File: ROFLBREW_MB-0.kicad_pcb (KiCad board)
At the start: 4 copper layers, 132.7 x 76 mm, 453 parts, among them P1 CONN_01X02, P10 CONN_01X02, P11 CONN_01X02, P12 CONN_01X02, P13 CONN_02X03, P14 CONN_01X02, P15 CONN_01X02, P16 CONN_01X02, P17 CONN_01X02, P18 CONN_01X02, P19 CONN_01X02, P2 CONN_01X02, P20 CONN_01X02, P21 CONN_02X20, P22 CONN_02X04, P23 CONN_02X04, P24 CONN_01X02, P25 CONN_01X02, P26 CONN_01X02, P27 CONN_01X02, P28 CONN_01X02, P29 CONN_01X02, P3 CONN_01X02, P30 CONN_01X02, P31 CONN_01X02, P4 CONN_01X02, P5 CONN_02X10, P6 CONN_01X02, P7 CONN_02X08, P8 CONN_01X02, P9 CONN_01X02, Q1 ASEM1, Q2 MUN5233T1G, Q3 ASTMTXK, U1 LT3480, U2 STM32F756ZGTx, U3 MAX31865, U4 MAX31865, U5 MAX31865, U6 MAX31865

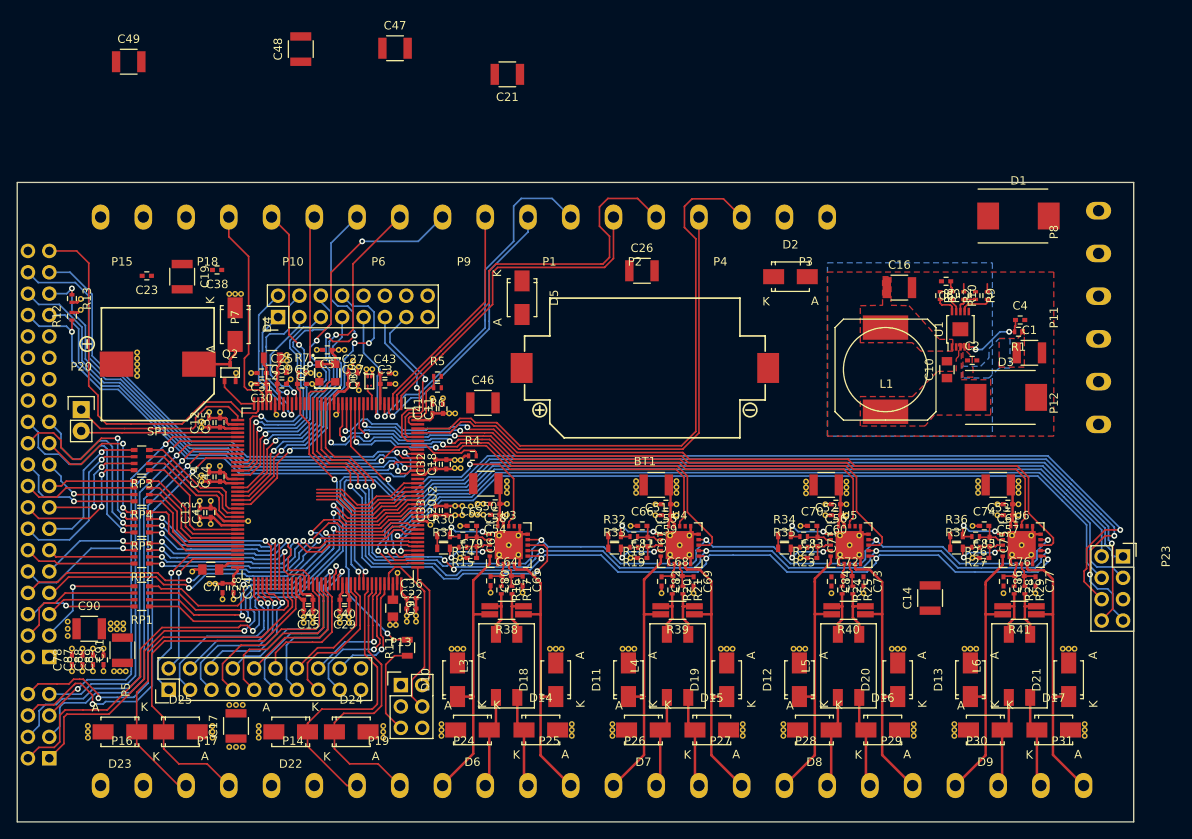
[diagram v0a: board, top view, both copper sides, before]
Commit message: Update some component footprints, add SD card and RTD power routing
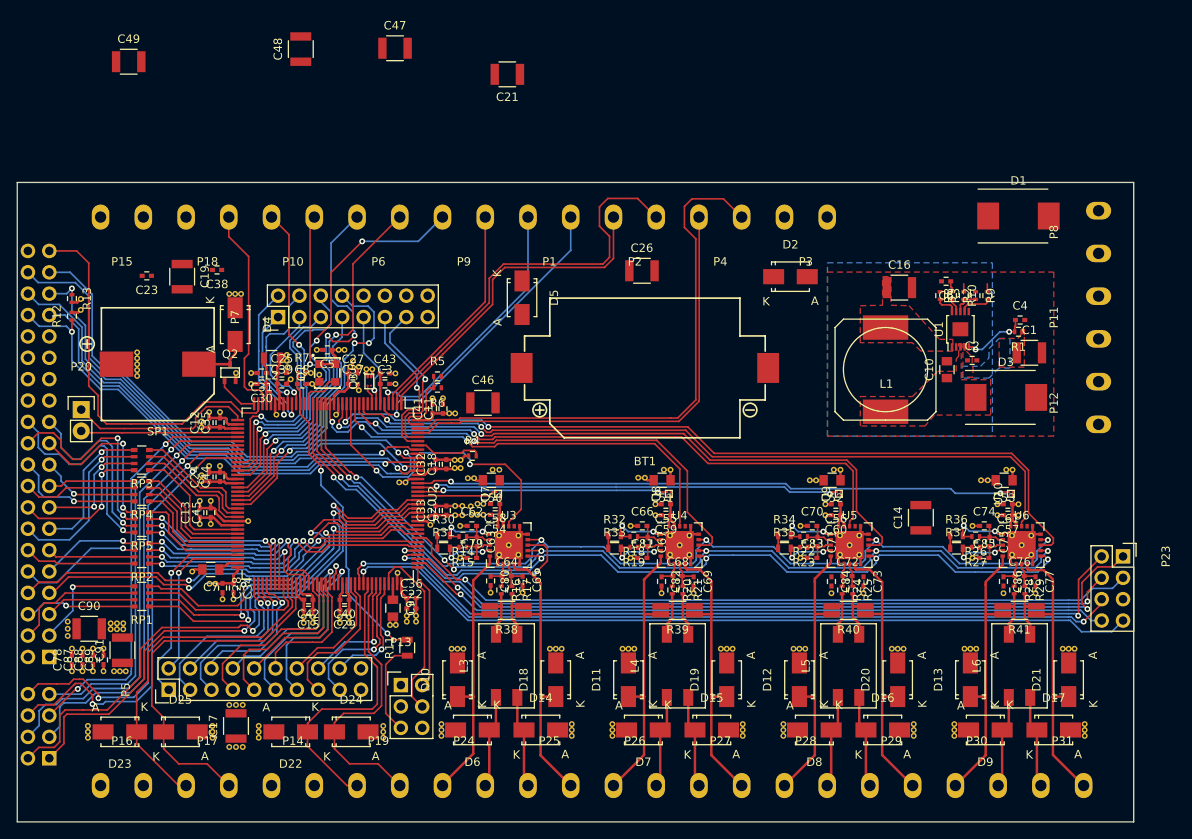
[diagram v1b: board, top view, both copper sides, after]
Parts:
- removed the REF** at (149.2, 101.9)
- removed the REF** at (128.8, 102.0)
- removed the REF** at (113.3, 101.7)
- removed the REF** at (108.5, 101.9)
- removed the REF** at (154.0, 102.4)
- removed the REF** at (154.0, 101.7)
- removed the REF** at (154.0, 101.0)
- removed the REF** at (133.6, 102.5)
- removed the REF** at (133.6, 101.8)
- removed the REF** at (133.6, 101.0)
- removed the REF** at (133.6, 105.0)
- removed the REF** at (133.6, 103.8)
- removed the REF** at (113.3, 105.0)
- removed the REF** at (113.3, 103.8)
- removed the REF** at (113.3, 102.4)
- removed the REF** at (113.3, 101.8)
- removed the REF** at (93.2, 104.5)
- removed the REF** at (93.2, 103.2)
- removed the REF** at (93.2, 100.5)
- added REF**: VIA-0.7x0.35, vias:VIA-0.7x0.35, F.Cu at (80.4, 100.7)
- added REF**: VIA-0.7x0.35, vias:VIA-0.7x0.35, F.Cu at (81.2, 100.7)
- added REF**: VIA-0.7x0.35, vias:VIA-0.7x0.35, F.Cu at (152.6, 99.2)
- added REF**: VIA-0.7x0.35, vias:VIA-0.7x0.35, F.Cu at (153.3, 99.2)
- added REF**: VIA-0.7x0.35, vias:VIA-0.7x0.35, F.Cu at (132.1, 99.2)
- added REF**: VIA-0.7x0.35, vias:VIA-0.7x0.35, F.Cu at (132.8, 99.2)
- added REF**: VIA-0.7x0.35, vias:VIA-0.7x0.35, F.Cu at (112.7, 99.2)
- added REF**: VIA-0.7x0.35, vias:VIA-0.7x0.35, F.Cu at (88.5, 100.2)
- added REF**: VIA-0.7x0.35, vias:VIA-0.7x0.35, F.Cu at (89.3, 100.2)
- added U10: TPS2290x, power_switches:TPS229x, F.Cu at (153.1, 102.0)
- added U7: TPS2290x, power_switches:TPS229x, F.Cu at (92.2, 102.0)
- added U8: TPS2290x, power_switches:TPS229x, F.Cu at (112.5, 102.0)
- added U9: TPS2290x, power_switches:TPS229x, F.Cu at (132.7, 102.0)
- C50, C51, C52, C53: value 22µ -> 1µ; footprint Capacitors_SMD:C_1210 -> Capacitors_SMD:C_0805
- moved C14 9.61 mm to (142.4, 104.8)
- moved REF** 2.89 mm to (92.3, 99.2)
- moved REF** 2.66 mm to (91.5, 99.2)
- moved REF** 2.02 mm to (111.8, 99.2)
- moved REF** 1.21 mm to (129.9, 100.4)
- moved REF** 1.15 mm to (150.3, 100.4)
- moved REF** 1.13 mm to (108.8, 100.1)
- moved REF** 1.12 mm to (109.6, 100.1)
- moved REF** 0.96 mm to (129.2, 100.4)
- moved C53 0.89 mm to (152.3, 100.4)
- moved C51 0.89 mm to (111.7, 100.4)
- moved C52 0.89 mm to (131.8, 100.4)
- moved REF** 0.87 mm to (149.6, 100.4)
- moved C50 0.76 mm to (91.3, 100.4)
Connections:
- C54 pad 1: +3V3 -> Net-(C54-Pad1)
- C55 pad 1: +3V3 -> Net-(C55-Pad1)
- C56 pad 1: +3V3 -> Net-(C56-Pad1)
- C57 pad 1: +3V3 -> Net-(C57-Pad1)
- C58 pad 1: +3V3 -> Net-(C54-Pad1)
- C59 pad 1: +3V3 -> Net-(C55-Pad1)
- C60 pad 1: +3V3 -> Net-(C56-Pad1)
- C61 pad 1: +3V3 -> Net-(C57-Pad1)
- P5 pad 19: /PG11 -> Net-(P5-Pad19)
- P5 pad 20: /PG12 -> Net-(P5-Pad20)
- P7 pad 10: /PG14 -> Net-(P7-Pad10)
- P7 pad 12: /PG13 -> Net-(P7-Pad12)
- U2 pad 126: /PG11 -> /RTD_PWR_0
- U2 pad 127: /PG12 -> /RTD_PWR_1
- U2 pad 128: /PG13 -> /RTD_PWR_2
- U2 pad 129: /PG14 -> /RTD_PWR_3
- U3 pad 19: +3V3 -> Net-(C54-Pad1)
- U3 pad 20: +3V3 -> Net-(C54-Pad1)
- U4 pad 19: +3V3 -> Net-(C55-Pad1)
- U4 pad 20: +3V3 -> Net-(C55-Pad1)
- U5 pad 19: +3V3 -> Net-(C56-Pad1)
- U5 pad 20: +3V3 -> Net-(C56-Pad1)
- U6 pad 19: +3V3 -> Net-(C57-Pad1)
- U6 pad 20: +3V3 -> Net-(C57-Pad1)
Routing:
- net /RTD_PWR_3: track 0.00 -> 71.1 mm, vias 0 -> 2
- net /RTD_PWR_2: track 0.00 -> 50.5 mm, vias 0 -> 2
- net /SD_D1: track 126.4 -> 95.7 mm, vias 3 -> 1
- net /SD_D0: track 124.7 -> 94.7 mm
- net /RTD_PWR_1: track 0.00 -> 29.8 mm, vias 0 -> 2
- net /SD_CARDD: track 112.6 -> 84.1 mm, vias 2 -> 1
- net +3V3: track 111.0 -> 86.9 mm
- net /PG14: track 13.8 -> 0.00 mm
- net /PG13: track 13.8 -> 0.00 mm
- net /PG12: track 13.7 -> 0.00 mm
- net /PG11: track 13.7 -> 0.00 mm
- net /SD_D2: track 103.2 -> 91.6 mm, vias 1 -> 2
- net /SD_CMD: track 99.7 -> 88.8 mm
- net GND: track 99.9 -> 109.6 mm
- net /RTD_PWR_0: track 0.00 -> 9.54 mm
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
